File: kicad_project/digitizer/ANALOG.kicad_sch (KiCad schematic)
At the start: 18 parts, among them IC301 ADS1234IPWR, J301 Load Cell 1, J302 Load Cell 2, J303 Load Cell 3

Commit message: finished ADC routing, including MCU pins (MUX, I2C, etc.)
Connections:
- removed net signal (+): C304.2, C306.1, C307.1, IC301.11 (AINP1), IC301.13 (AINP3), IC301.18 (AINP2), J301.4, J302.4, J303.4
- removed net signal (-): C304.1, C306.2, C307.2, IC301.12 (AINN1), IC301.14 (AINN3), IC301.17 (AINN2), J301.5, J302.5, J303.5
- new net load cell 1 - signal (+): C306.1, IC301.11 (AINP1), J301.4
- new net load cell 1 - signal (-): C306.2, IC301.12 (AINN1), J301.5
- new net load cell 2 - signal (+): C307.1, IC301.13 (AINP3), J302.4
- new net load cell 2 - signal (-): C307.2, IC301.14 (AINN3), J302.5
- new net load cell 3 - signal (+): C304.2, IC301.18 (AINP2), J303.4
- new net load cell 3 - signal (-): C304.1, IC301.17 (AINN2), J303.5
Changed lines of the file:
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@@
     (effects (font (size 1.27 1.27)) (justify left bottom))
   )
-  (label "signal (+)" (at 64.77 54.61 0)
+  (label "load cell 1 - signal (+)" (at 64.77 54.61 0)
     (effects (font (size 1.27 1.27)) (justify left bottom))
   )
-  (label "signal (-)" (at 64.77 130.81 0)
+  (label "load cell 3 - signal (-)" (at 64.77 130.81 0)
     (effects (font (size 1.27 1.27)) (justify left bottom))
   )
-  (label "signal (+)" (at 64.77 133.35 0)
+  (label "load cell 3 - signal (+)" (at 64.77 133.35 0)
     (effects (font (size 1.27 1.27)) (justify left bottom))
   )
@@
     (effects (font (size 1.27 1.27)) (justify left bottom))
   )
-  (label "signal (+)" (at 64.77 92.71 0)
+  (label "load cell 2 - signal (+)" (at 64.77 92.71 0)
     (effects (font (size 1.27 1.27)) (justify left bottom))
   )
@@
     (effects (font (size 1.27 1.27)) (justify left bottom))
   )
-  (label "signal (-)" (at 64.77 90.17 0)
+  (label "load cell 2 - signal (-)" (at 64.77 90.17 0)
     (effects (font (size 1.27 1.27)) (justify left bottom))
   )
@@
     (effects (font (size 1.27 1.27)) (justify left bottom))
   )
-  (label "signal (-)" (at 64.77 52.07 0)
+  (label "load cell 1 - signal (-)" (at 64.77 52.07 0)
     (effects (font (size 1.27 1.27)) (justify left bottom))
   )

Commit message: updated schematic to use all 0805 parts (both caps and resistors)
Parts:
- C301, C302, C303, C304, C305, C306, C307: footprint Capacitor_SMD:C_2220_5650Metric_Pad1.97x5.40mm_HandSolder -> Capacitor_SMD:C_0805_2012Metric_Pad1.18x1.45mm_HandSolder
- R301, R302, R303, R304, R305, R306, R307: footprint Resistor_SMD:R_2512_6332Metric_Pad1.40x3.35mm_HandSolder -> Resistor_SMD:R_0805_2012Metric_Pad1.20x1.40mm_HandSolder
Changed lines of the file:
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@@
       (effects (font (size 1.27 1.27)) (justify left))
     )
-    (property "Footprint" "Resistor_SMD:R_2512_6332Metric_Pad1.40x3.35mm_HandSolder" (id 2) (at 163.83 74.93 0)
+    (property "Footprint" "Resistor_SMD:R_0805_2012Metric_Pad1.20x1.40mm_HandSolder" (id 2) (at 163.83 74.93 0)
       (effects (font (size 1.27 1.27)) hide)
     )
@@
       (effects (font (size 1.27 1.27)) (justify left))
     )
-    (property "Footprint" "Capacitor_SMD:C_2220_5650Metric_Pad1.97x5.40mm_HandSolder" (id 2) (at 104.14 95.25 0)
+    (property "Footprint" "Capacitor_SMD:C_0805_2012Metric_Pad1.18x1.45mm_HandSolder" (id 2) (at 104.14 95.25 0)
       (effects (font (size 1.27 1.27)) hide)
     )
@@
       (effects (font (size 1.27 1.27)) (justify left))
     )
-    (property "Footprint" "Resistor_SMD:R_2512_6332Metric_Pad1.40x3.35mm_HandSolder" (id 2) (at 148.59 35.56 0)
+    (property "Footprint" "Resistor_SMD:R_0805_2012Metric_Pad1.20x1.40mm_HandSolder" (id 2) (at 148.59 35.56 0)
       (effects (font (size 1.27 1.27)) hide)
     )
@@
       (effects (font (size 1.27 1.27)) (justify left))
     )
-    (property "Footprint" "Resistor_SMD:R_2512_6332Metric_Pad1.40x3.35mm_HandSolder" (id 2) (at 181.61 72.39 0)
+    (property "Footprint" "Resistor_SMD:R_0805_2012Metric_Pad1.20x1.40mm_HandSolder" (id 2) (at 181.61 72.39 0)
       (effects (font (size 1.27 1.27)) hide)
     )
@@
       (effects (font (size 1.27 1.27)) (justify right))
     )
-    (property "Footprint" "Capacitor_SMD:C_2220_5650Metric_Pad1.97x5.40mm_HandSolder" (id 2) (at 194.31 67.31 0)
+    (property "Footprint" "Capacitor_SMD:C_0805_2012Metric_Pad1.18x1.45mm_HandSolder" (id 2) (at 194.31 67.31 0)
       (effects (font (size 1.27 1.27)) hide)
     )
@@
       (effects (font (size 1.27 1.27)) (justify left))
     )
-    (property "Footprint" "Capacitor_SMD:C_2220_5650Metric_Pad1.97x5.40mm_HandSolder" (id 2) (at 93.98 83.82 0)
+    (property "Footprint" "Capacitor_SMD:C_0805_2012Metric_Pad1.18x1.45mm_HandSolder" (id 2) (at 93.98 83.82 0)
       (effects (font (size 1.27 1.27)) hide)
     )
@@
       (effects (font (size 1.27 1.27)) (justify left))
     )
-    (property "Footprint" "Resistor_SMD:R_2512_6332Metric_Pad1.40x3.35mm_HandSolder" (id 2) (at 109.22 31.75 0)
+    (property "Footprint" "Resistor_SMD:R_0805_2012Metric_Pad1.20x1.40mm_HandSolder" (id 2) (at 109.22 31.75 0)
       (effects (font (size 1.27 1.27)) hide)
     )
@@
       (effects (font (size 1.27 1.27)) (justify left))
     )
-    (property "Footprint" "Resistor_SMD:R_2512_6332Metric_Pad1.40x3.35mm_HandSolder" (id 2) (at 153.67 43.18 0)
+    (property "Footprint" "Resistor_SMD:R_0805_2012Metric_Pad1.20x1.40mm_HandSolder" (id 2) (at 153.67 43.18 0)
       (effects (font (size 1.27 1.27)) hide)
     )
@@
       (effects (font (size 1.27 1.27)) (justify right))
     )
-    (property "Footprint" "Capacitor_SMD:C_2220_5650Metric_Pad1.97x5.40mm_HandSolder" (id 2) (at 189.23 80.01 0)
+    (property "Footprint" "Capacitor_SMD:C_0805_2012Metric_Pad1.18x1.45mm_HandSolder" (id 2) (at 189.23 80.01 0)
       (effects (font (size 1.27 1.27)) hide)
     )
@@
       (effects (font (size 1.27 1.27)) (justify left))
     )
-    (property "Footprint" "Capacitor_SMD:C_2220_5650Metric_Pad1.97x5.40mm_HandSolder" (id 2) (at 96.52 73.66 0)
+    (property "Footprint" "Capacitor_SMD:C_0805_2012Metric_Pad1.18x1.45mm_HandSolder" (id 2) (at 96.52 73.66 0)
       (effects (font (size 1.27 1.27)) hide)
     )
@@
       (effects (font (size 1.27 1.27)) (justify left))
     )
-    (property "Footprint" "Resistor_SMD:R_2512_6332Metric_Pad1.40x3.35mm_HandSolder" (id 2) (at 151.13 39.37 0)
+    (property "Footprint" "Resistor_SMD:R_0805_2012Metric_Pad1.20x1.40mm_HandSolder" (id 2) (at 151.13 39.37 0)
       (effects (font (size 1.27 1.27)) hide)
     )
@@
       (effects (font (size 1.27 1.27)) (justify left))
     )
-    (property "Footprint" "Capacitor_SMD:C_2220_5650Metric_Pad1.97x5.40mm_HandSolder" (id 2) (at 97.79 57.15 0)
+    (property "Footprint" "Capacitor_SMD:C_0805_2012Metric_Pad1.18x1.45mm_HandSolder" (id 2) (at 97.79 57.15 0)
       (effects (font (size 1.27 1.27)) hide)
     )
@@
       (effects (font (size 1.27 1.27)) (justify left))
     )
-    (property "Footprint" "Capacitor_SMD:C_2220_5650Metric_Pad1.97x5.40mm_HandSolder" (id 2) (at 180.34 80.01 0)
+    (property "Footprint" "Capacitor_SMD:C_0805_2012Metric_Pad1.18x1.45mm_HandSolder" (id 2) (at 180.34 80.01 0)
       (effects (font (size 1.27 1.27)) hide)
     )
@@
     (property "Reference" "R301" (id 0) (at 106.68 25.4 90))
     (property "Value" "47" (id 1) (at 111.76 25.4 90))
-    (property "Footprint" "Resistor_SMD:R_2512_6332Metric_Pad1.40x3.35mm_HandSolder" (id 2) (at 110.49 27.94 0)
-      (effects (font (size 1.27 1.27)) hide)
-    )
+    (property "Footprint" "Resistor_SMD:R_0805_2012Metric_Pad1.20x1.40mm_HandSolder" (id 2) (at 110.49 27.94 0)
+      (effects (font (size 1.27 1.27)) hide)
+    )

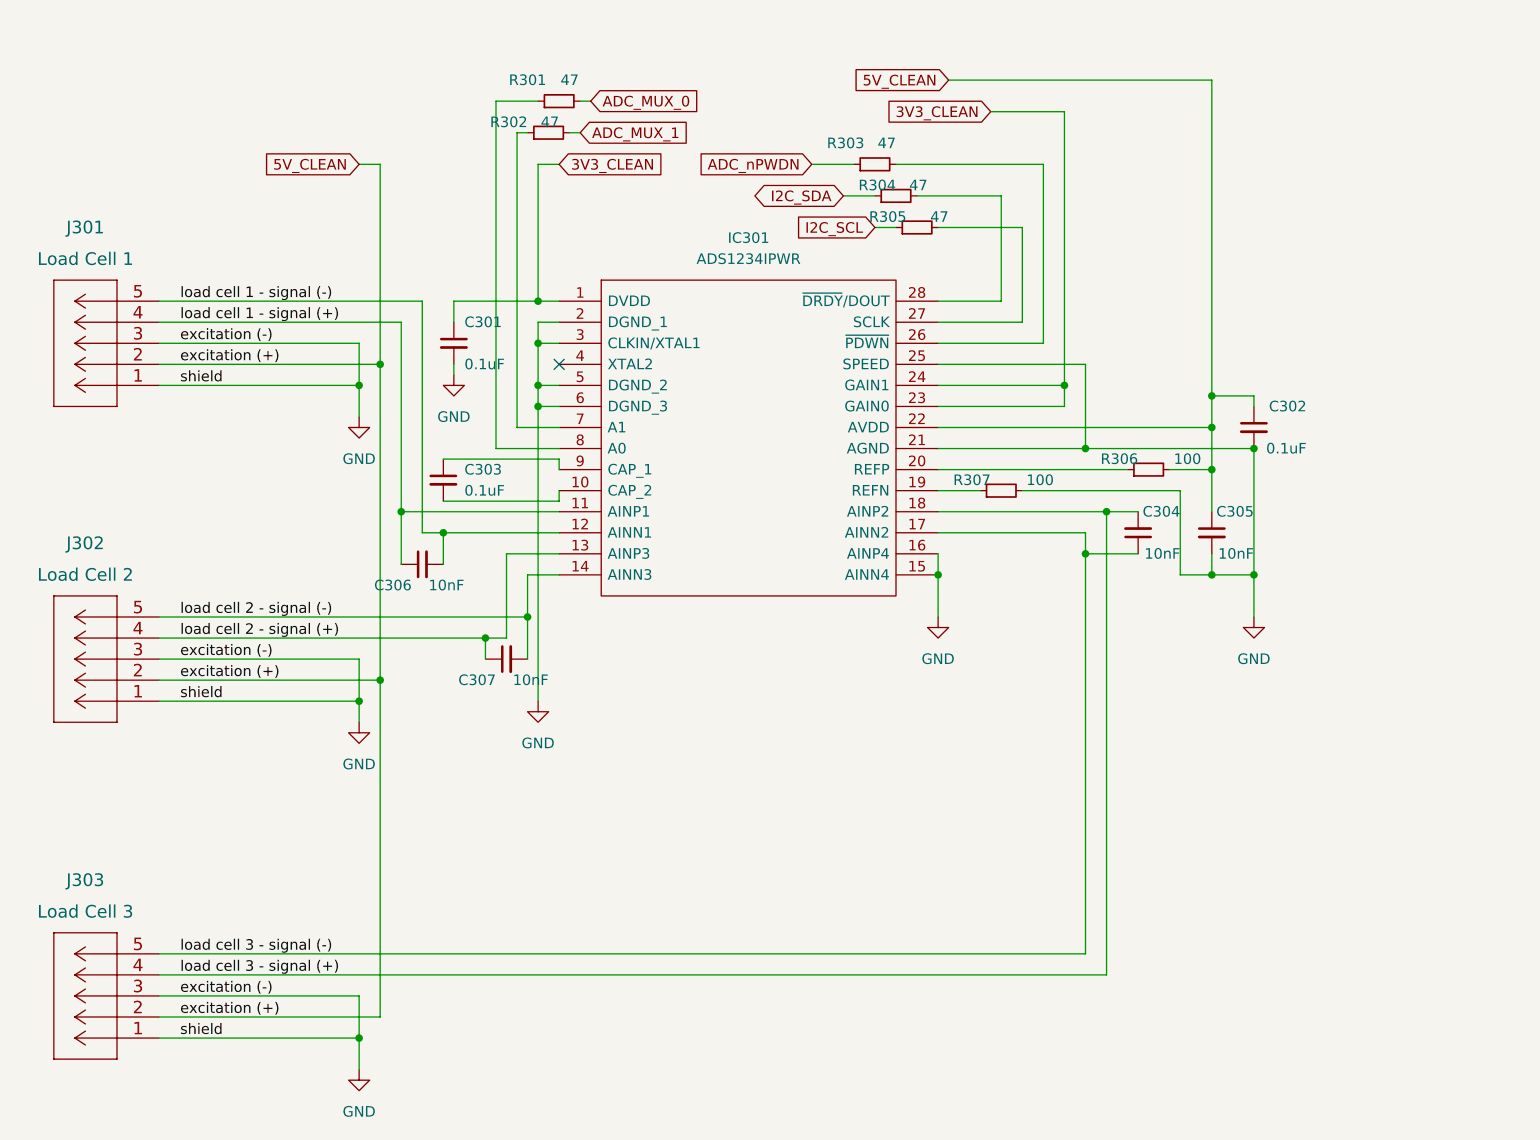
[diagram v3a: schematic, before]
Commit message: added 100ohm resistors to the differential analog inputs
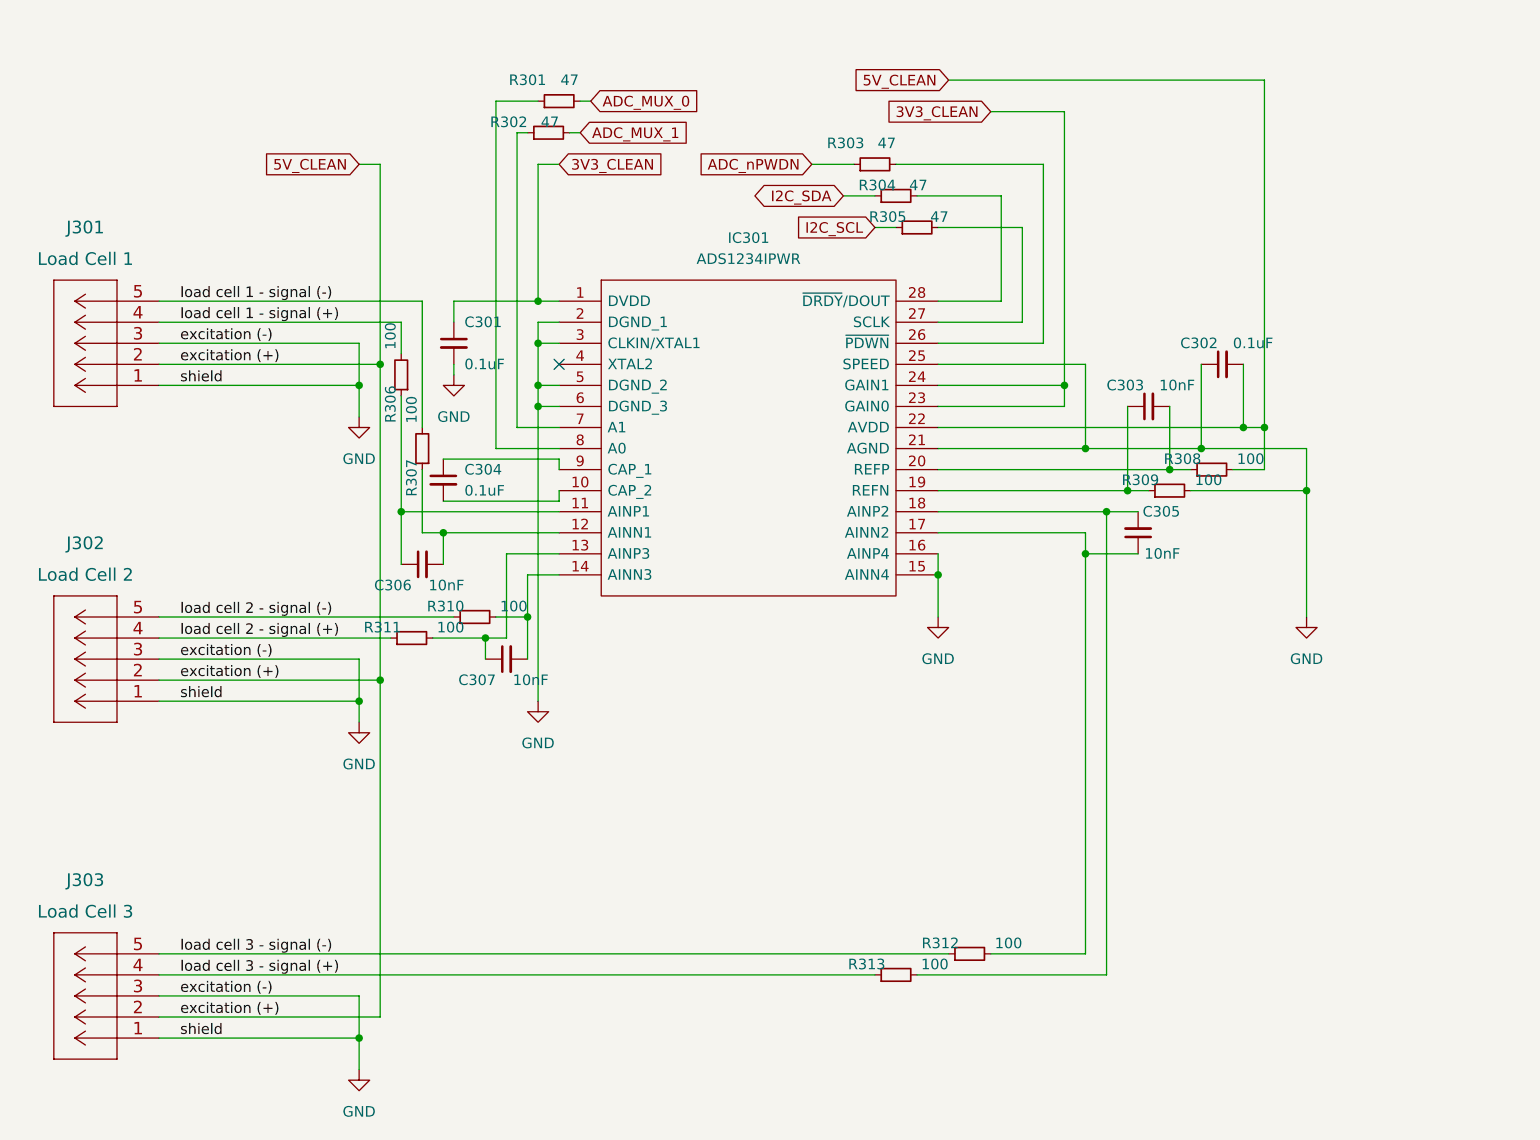
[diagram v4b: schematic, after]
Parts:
- added R306, R307, R310, R311, R312, R313: 100, Resistor_SMD:R_0805_2012Metric_Pad1.20x1.40mm_HandSolder, symbol Device:R_Small
- renumbered C305 to C303, C303 to C304, C304 to C305, R306 to R308, R307 to R309
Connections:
- net 5V_CLEAN: now also C302.2; no longer C302.1, C303.1
- net GND: now also C302.1; no longer C302.2, C303.2
- net load cell 1 - signal (+): now also R306.2; no longer C306.1, IC301.11 (AINP1)
- net load cell 1 - signal (-): now also R307.2; no longer C306.2, IC301.12 (AINN1)
- net load cell 2 - signal (+): now also R311.1; no longer C307.1, IC301.13 (AINP3)
- net load cell 2 - signal (-): now also R310.1; no longer C307.2, IC301.14 (AINN3)
- net load cell 3 - signal (+): now also R313.1; no longer C305.2, IC301.18 (AINP2)
- net load cell 3 - signal (-): now also R312.1; no longer C305.1, IC301.17 (AINN2)
- net at IC301.19 (REFN), R309.1: now also C303.1
- net at IC301.20 (REFP), R308.1: now also C303.2
- new net: C307.1, IC301.13 (AINP3), R311.2
- new net: C307.2, IC301.14 (AINN3), R310.2
- new net: C306.1, IC301.11 (AINP1), R306.1
- new net: C306.2, IC301.12 (AINN1), R307.1
- new net: C305.1, IC301.17 (AINN2), R312.2
- new net: C305.2, IC301.18 (AINP2), R313.2
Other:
- moved on the sheet: C302, C303, R308, R309

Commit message: added some 0R resistors to pads to allow for easier board modding
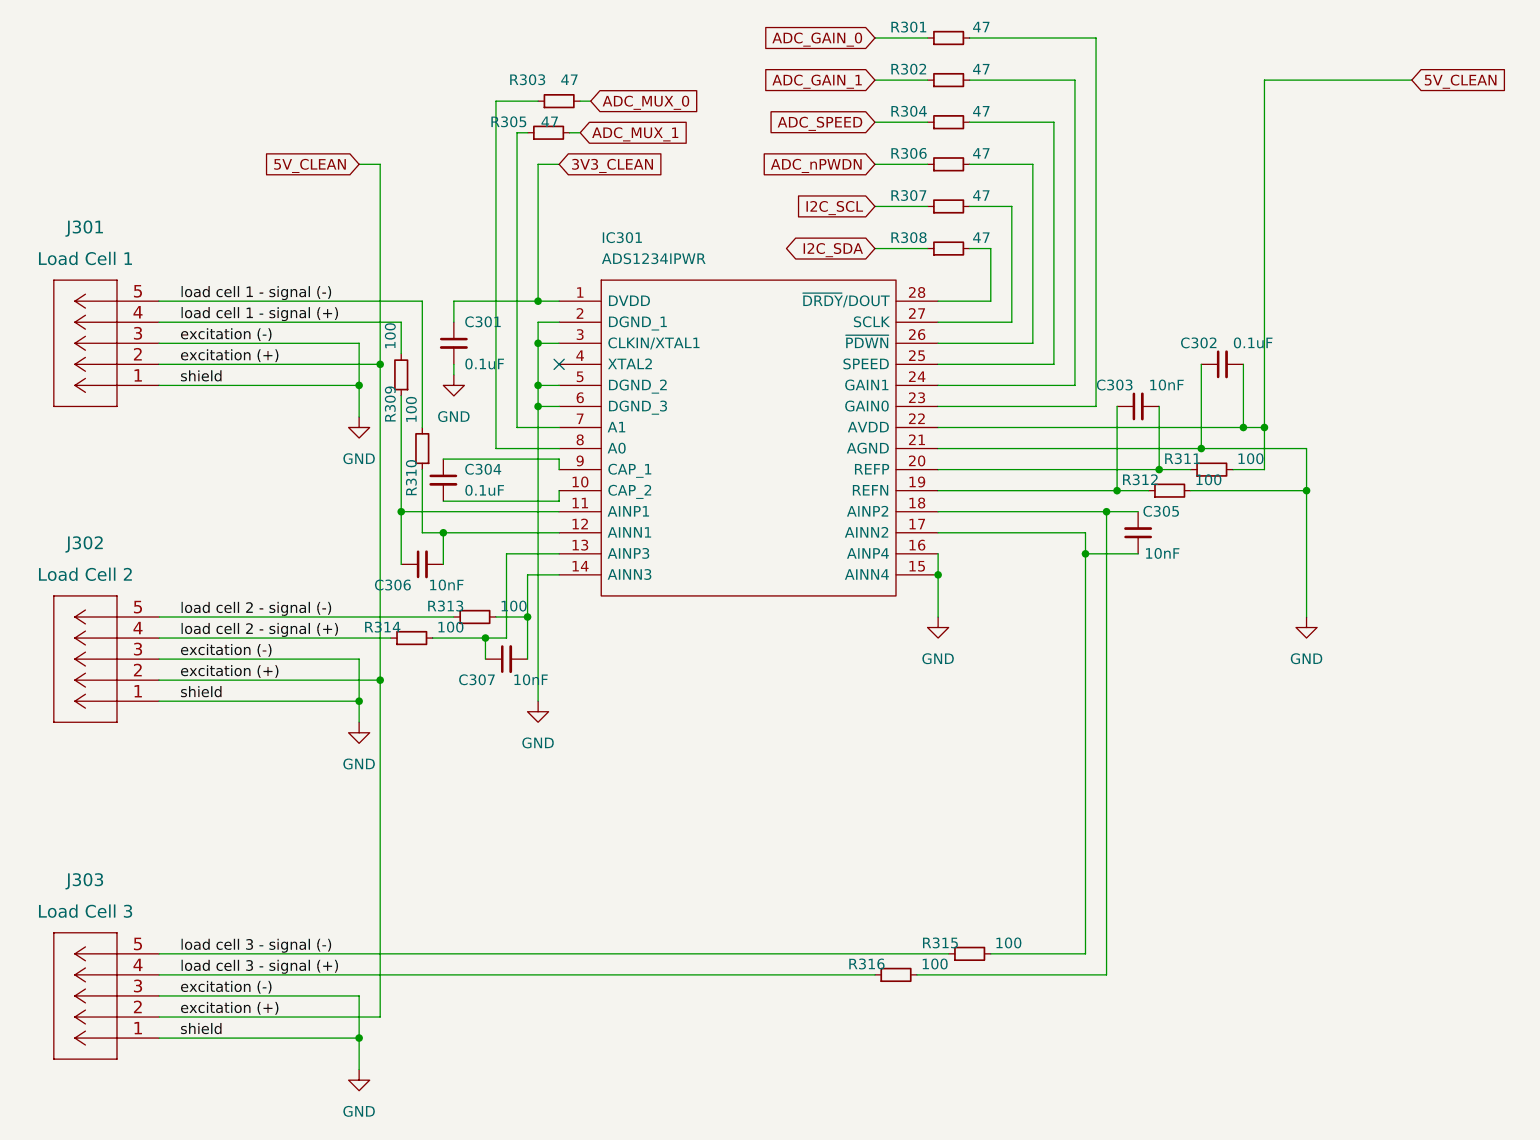
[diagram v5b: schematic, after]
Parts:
- added R301, R302, R304: 47, Resistor_SMD:R_0805_2012Metric_Pad1.20x1.40mm_HandSolder, symbol Device:R_Small
- renumbered R301 to R303, R302 to R305, R303 to R306, R305 to R307, R304 to R308, R306 to R309, R307 to R310, R308 to R311, R309 to R312, R310 to R313, R311 to R314, R312 to R315, R313 to R316
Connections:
- net 3V3_CLEAN: no longer IC301.23 (GAIN0), IC301.24 (GAIN1)
- net GND: no longer IC301.25 (SPEED)
- new net: IC301.24 (GAIN1), R302.2
- new net: IC301.25 (SPEED), R304.2
- new net: IC301.23 (GAIN0), R301.2
- new net ADC_GAIN_0: R301.1
- new net ADC_GAIN_1: R302.1
- new net ADC_SPEED: R304.1
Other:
- moved on the sheet: C303, R306, R307, R308
